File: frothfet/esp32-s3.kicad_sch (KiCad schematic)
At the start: 47 parts, among them J3 USB_TYPE_C_16PIN, Q20 FDC6330L, Q21 S8050, Q22 S8050, SW1 RESET, SW2 BOOT, U31 ESP32-S3-WROOM-1-N16R8, U32 USBLC6-2SC6, U33 XC6210B332MR, U34 CH334F, U35 CH343P, Y1 12Mhz, Y2 32.768kHz

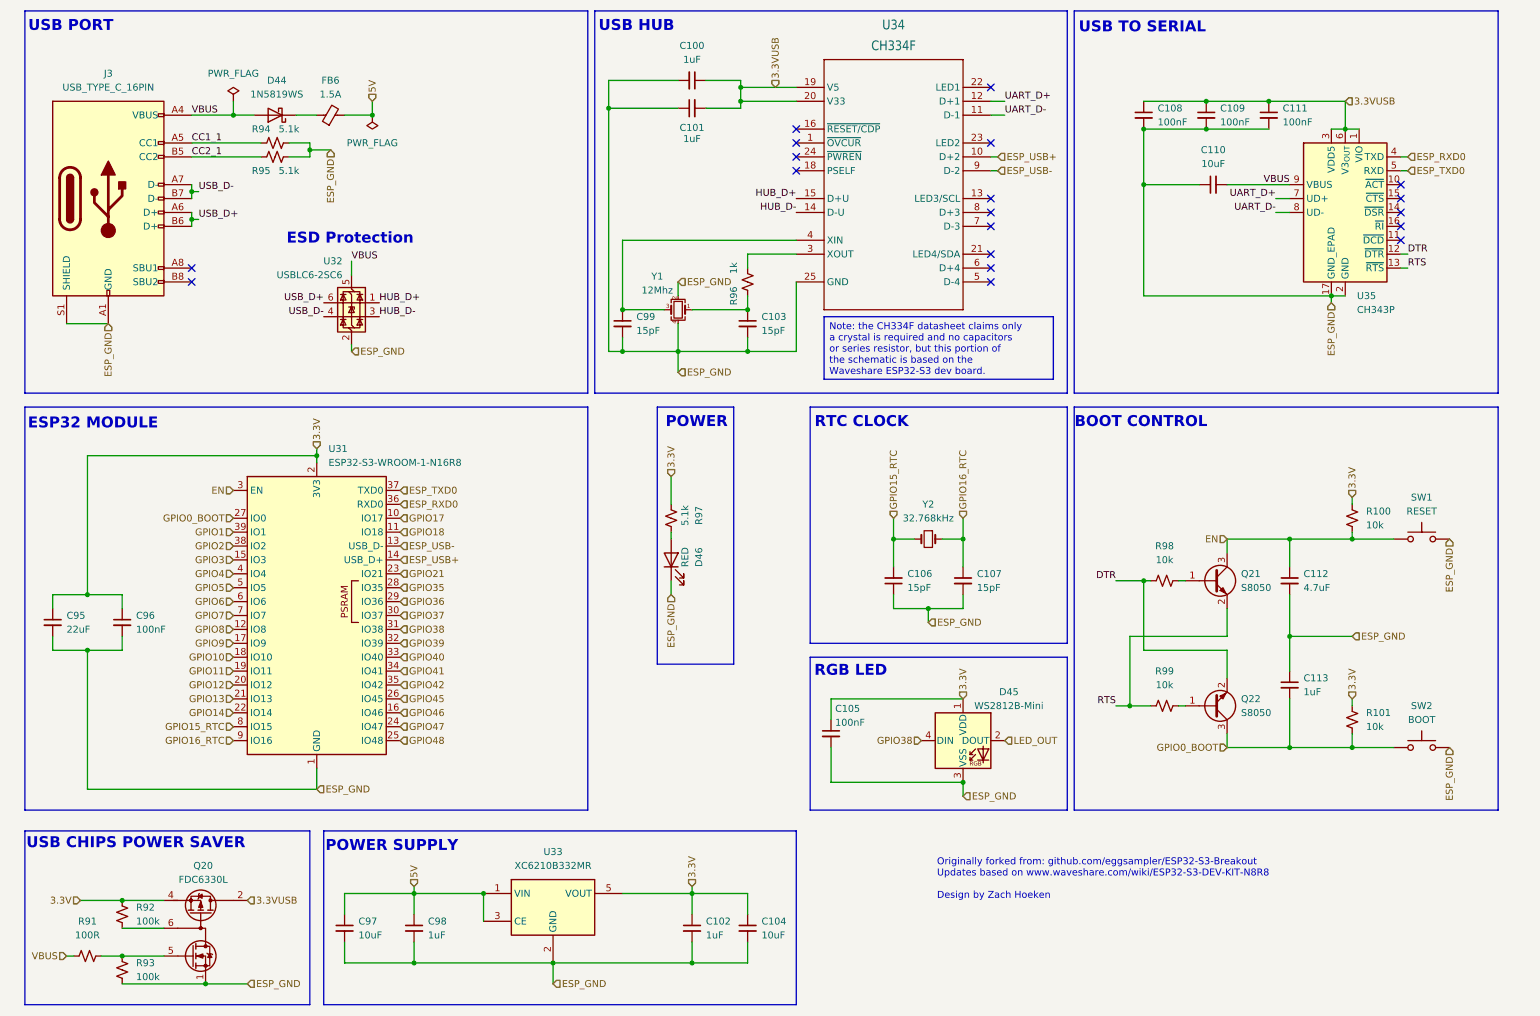
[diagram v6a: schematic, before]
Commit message: pulled in updated esp32-s3 schematic
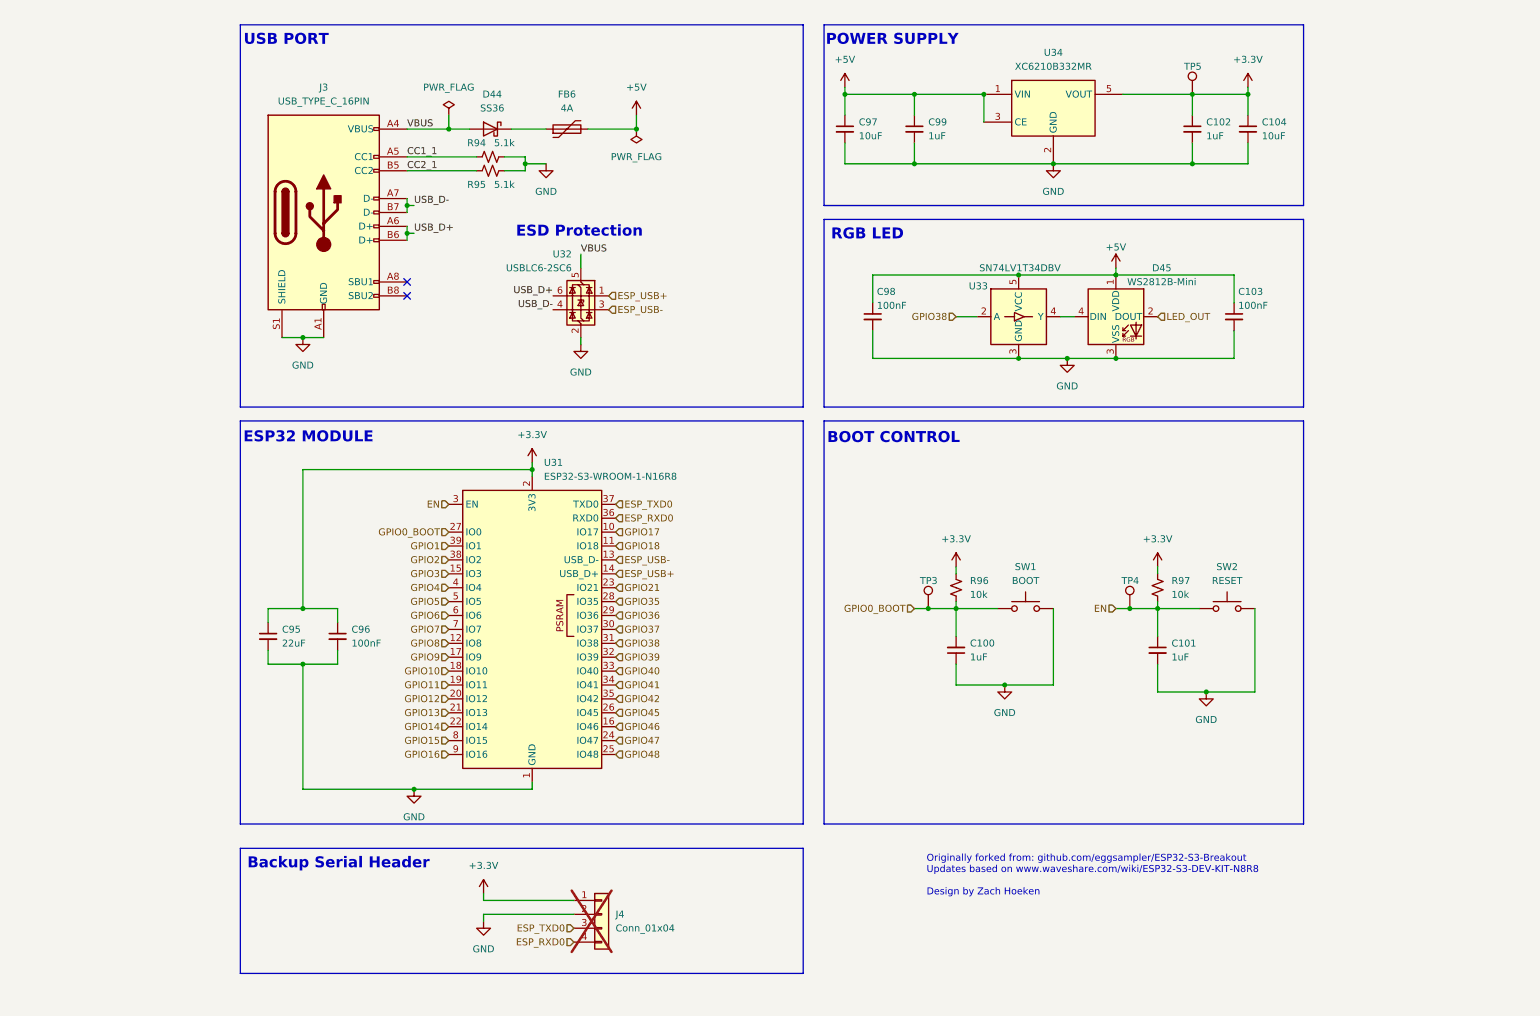
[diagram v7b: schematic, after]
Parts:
- removed C100, C101: 1uF, Capacitor_SMD:C_0603_1608Metric, symbol Device:C_Small
- removed C106, C107, C99: 15pF, Capacitor_SMD:C_0603_1608Metric, symbol Device:C_Small
- removed C108, C109, C111: 100nF, Capacitor_SMD:C_0603_1608Metric, symbol Device:C_Small
- removed C110: 10uF, Capacitor_SMD:C_0603_1608Metric, symbol Device:C_Small
- removed D44: 1N5819WS, Diode_SMD:D_SOD-323, symbol Diode:1N5819WS
- removed D46: RED, LED_SMD:LED_0603_1608Metric, symbol Device:LED
- removed Q20: FDC6330L, Package_TO_SOT_SMD:TSOT-23-6, symbol Transistor_FET:FDC6330L
- removed Q21, Q22: S8050, Package_TO_SOT_SMD:SOT-23, symbol Transistor_BJT:Q_NPN_BEC
- removed R91: 100R, Resistor_SMD:R_0603_1608Metric, symbol Device:R_Small_US
- removed R92, R93: 100k, Resistor_SMD:R_0603_1608Metric, symbol Device:R_Small_US
- removed R96: 1k, Resistor_SMD:R_0603_1608Metric, symbol Device:R_Small_US
- removed R97: 5.1k, Resistor_SMD:R_0603_1608Metric, symbol Device:R_Small_US
- removed R98, R99: 10k, Resistor_SMD:R_0603_1608Metric, symbol Device:R_Small_US
- removed U34: CH334F, yarrboard:QFN-24-1EP_4x4mm_P0.5mm_EP2.7x2.7mm_ThermalVias, symbol yarrboard:CH334F
- removed U35: CH343P, yarrboard:QFN-16-1EP_3x3mm_P0.5mm_EP1.7x1.7mm_ThermalVias, symbol Interface_USB:CH343P
- removed Y1: 12Mhz, Crystal:Crystal_SMD_SeikoEpson_TSX3225-4Pin_3.2x2.5mm, symbol Device:Crystal_GND24_Small
- removed Y2: 32.768kHz, Crystal:Crystal_SMD_3215-2Pin_3.2x1.5mm, symbol Device:Crystal_Small
- added D44: SS36, Diode_SMD:D_SMA, symbol Diode:SS36
- added J4: Conn_01x04, Connector_PinHeader_2.54mm:PinHeader_1x04_P2.54mm_Vertical_SMD_Pin1Left, symbol Connector_Generic:Conn_01x04
- added TP3, TP4, TP5: ~, TestPoint:TestPoint_THTPad_D1.5mm_Drill0.7mm, symbol Connector:TestPoint
- added U33: SN74LV1T34DBV, Package_TO_SOT_SMD:SOT-23-5, symbol Logic_LevelTranslator:SN74LV1T34DBV
- C101: renamed from C112; value 4.7uF -> 1uF
- C103: value 15pF -> 100nF
- FB6: value 1.5A -> 4A; symbol Device:FerriteBead_Small -> Device:Polyfuse; LCSC C2760275 -> C2760306
- SW1: renamed from SW2; footprint Button_Switch_THT:SW_Tactile_SPST_Angled_PTS645Vx58-2LFS -> Button_Switch_SMD:SW_SPST_B3U-1000P; LCSC C557599 -> C231329; Rotation Offset 180 -> 90
- SW2: renamed from SW1; footprint Button_Switch_THT:SW_Tactile_SPST_Angled_PTS645Vx58-2LFS -> Button_Switch_SMD:SW_SPST_B3U-1000P; LCSC C557599 -> C231329; Rotation Offset 180 -> 90
- renumbered C113 to C100, C105 to C98, C98 to C99, R101 to R96, R100 to R97, U33 to U34
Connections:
- net 5V is gone; now on net +5V: C97.1, C99.1, FB6.2, U34.1 (VIN), U34.3 (CE)
- net HUB_D+ is gone; now on net ESP_USB+: U32.1 (I/O1)
- net HUB_D- is gone; now on net ESP_USB-: U32.3 (I/O2)
- net EN: now also TP4.1
- net ESP_RXD0: now also J4.4 (Pin_4)
- net ESP_TXD0: now also J4.3 (Pin_3)
- net GPIO0_BOOT: now also TP3.1
- net GPIO38: now also U33.2 (A); no longer D45.4 (DIN)
- net VBUS: now also D44.2 (A)
- net +5V: now reaches C103.1
- net +5V: now also C98.1, D45.1 (VDD), U33.5 (VCC)
- net at FB6.1: now also D44.1 (K)
- net 3.3V renamed +3.3V
- net +3.3V: now also J4.1 (Pin_1), TP5.1; no longer C98.1, D45.1 (VDD)
- net ESP_GND renamed GND
- net GND: now also J4.2 (Pin_2), U33.3 (GND)
- net GPIO15_RTC renamed GPIO15
- net GPIO16_RTC renamed GPIO16
- new net: D45.4 (DIN), U33.4 (Y)
- no-connect marks 19 -> 2
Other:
- note added: "Backup Serial Header"
- note removed: "POWER"
- note removed: "RTC CLOCK"
- note removed: "USB CHIPS POWER SAVER"
- note removed: "USB HUB"
- note removed: "USB TO SERIAL"
- title: https://github.com/hoeken/ESP32-S3-Template -> https://github.com/hoeken/brineomatic
- moved on the sheet: C100, C101, C102, C104, C95, C96, C97, C98, C99, D45, FB6, J3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

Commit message: wired the i2c addresses.
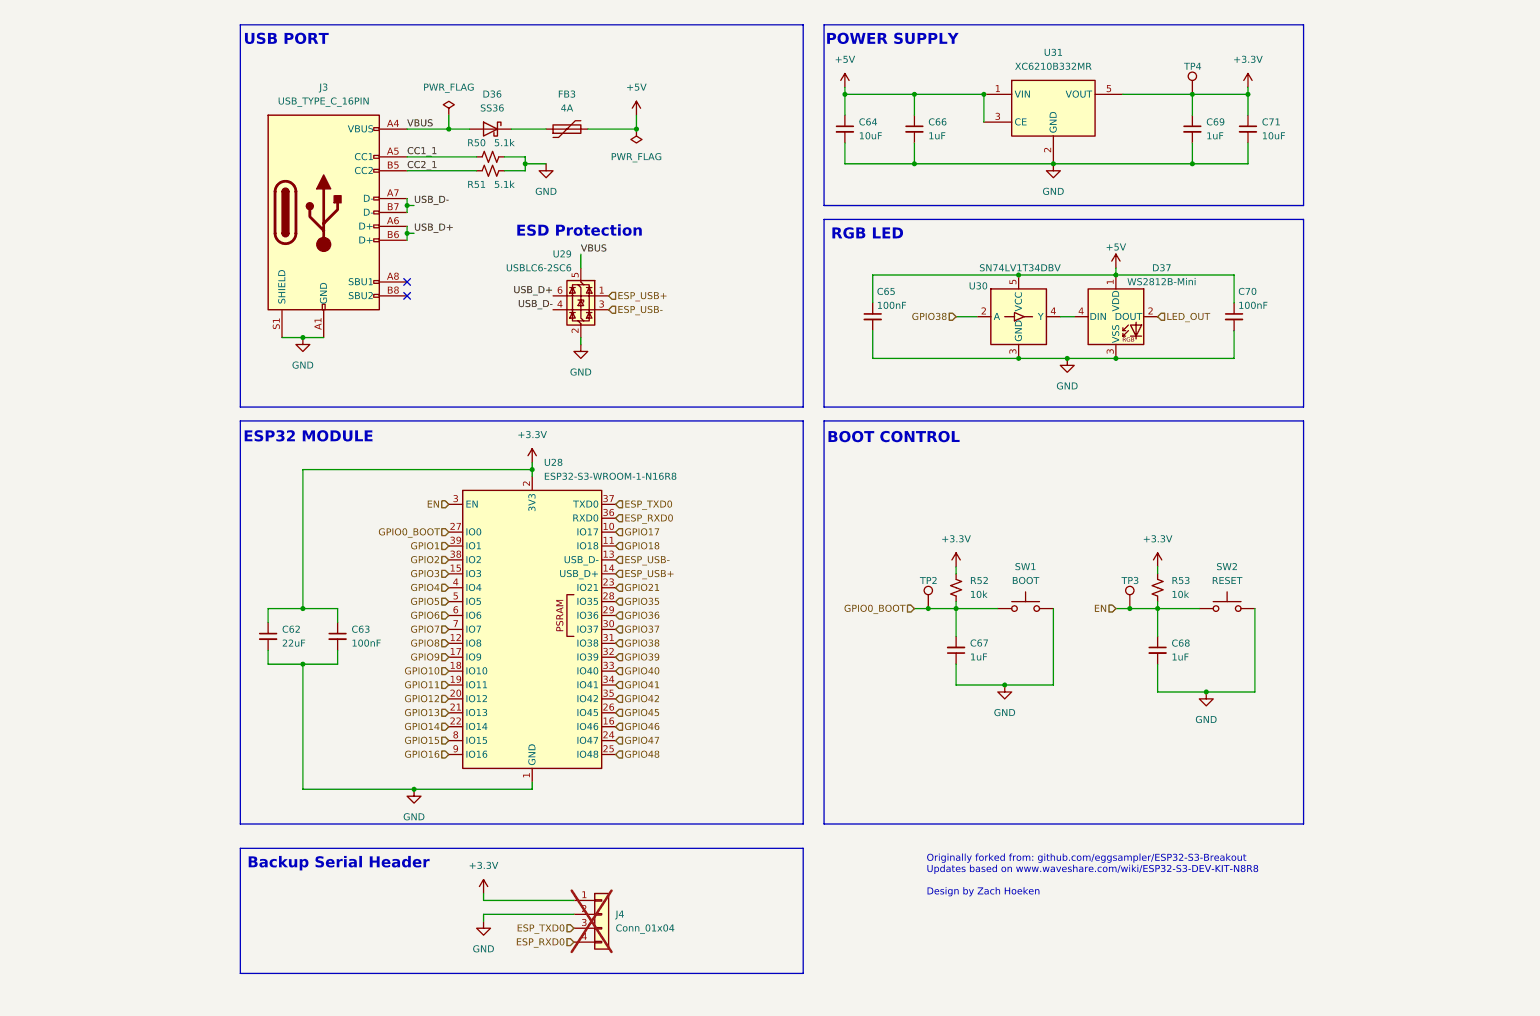
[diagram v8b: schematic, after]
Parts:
- renumbered C95 to C62, C96 to C63, C97 to C64, C98 to C65, C99 to C66, C100 to C67, C101 to C68, C102 to C69, C103 to C70, C104 to C71, D44 to D36, D45 to D37, FB6 to FB3, R94 to R50, R95 to R51, R96 to R52, R97 to R53, TP3 to TP2, TP4 to TP3, TP5 to TP4, U31 to U28, U32 to U29, U33 to U30, U34 to U31
